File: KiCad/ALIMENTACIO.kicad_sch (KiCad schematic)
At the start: 13 parts, among them J1 Conn_01x02_Pin, U1 LM2596S-5, U2 LM1117DT-3.3

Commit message: Modificacio
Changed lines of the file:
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@@
-	)
-	(junction
-		(at 64.77 99.06)
-		(diameter 0)
-		(color 0 0 0 0)
 	)
 	(junction
@@
 	)
 	(junction
+		(at 60.96 99.06)
+		(diameter 0)
+		(color 0 0 0 0)
+	)
+	(junction
 		(at 176.53 104.14)
+		(diameter 0)
+		(color 0 0 0 0)
+	)
+	(junction
+		(at 60.96 101.6)
 		(diameter 0)
 		(color 0 0 0 0)
@@
 	(wire
 		(pts
-			(xy 57.15 99.06) (xy 64.77 99.06)
+			(xy 57.15 99.06) (xy 60.96 99.06)
 		)
 		(stroke
@@
 	(wire
 		(pts
+			(xy 60.96 101.6) (xy 57.15 101.6)
+		)
+		(stroke
+			(width 0)
+			(type default)
+		)
+	)
+	(wire
+		(pts
 			(xy 245.11 104.14) (xy 259.08 104.14)
 		)
@@
 	(wire
 		(pts
+			(xy 60.96 99.06) (xy 78.74 99.06)
+		)
+		(stroke
+			(width 0)
+			(type default)
+		)
+	)
+	(wire
+		(pts
 			(xy 231.14 111.76) (xy 231.14 119.38)
 		)
@@
 	(wire
 		(pts
+			(xy 64.77 101.6) (xy 60.96 101.6)
+		)
+		(stroke
+			(width 0)
+			(type default)
+		)
+	)
+	(wire
+		(pts
 			(xy 99.06 99.06) (xy 109.22 99.06)
 		)
@@
 		(pts
 			(xy 143.51 99.06) (xy 176.53 99.06)
-		)
-		(stroke
-			(width 0)
-			(type default)
-		)
-	)
-	(wire
-		(pts
-			(xy 64.77 99.06) (xy 78.74 99.06)
 		)
 		(stroke
@@
 	(global_label "GND"
 		(shape input)
-		(at 57.15 101.6 0)
+		(at 64.77 101.6 0)
 		(fields_autoplaced yes)
 		(effects
@@
 		)
 		(property "Intersheetrefs" "${INTERSHEET_REFS}"
-			(at 64.0057 101.6 0)
+			(at 71.6257 101.6 0)
 			(effects
 				(font
@@
 	(symbol
 		(lib_id "power:PWR_FLAG")
-		(at 64.77 99.06 0)
+		(at 60.96 99.06 0)
 		(unit 1)
 		(exclude_from_sim no)
@@
 		(fields_autoplaced yes)
 		(property "Reference" "#FLG01"
-			(at 64.77 97.155 0)
+			(at 60.96 97.155 0)
 			(effects
 				(font
@@
 		)
 		(property "Value" "PWR_FLAG"
-			(at 64.77 93.98 0)
+			(at 60.96 93.98 0)
 			(effects
 				(font
@@
 		)
 		(property "Footprint" ""
-			(at 64.77 99.06 0)
+			(at 60.96 99.06 0)
 			(effects
 				(font
@@
 		)
 		(property "Datasheet" "~"
-			(at 64.77 99.06 0)
+			(at 60.96 99.06 0)
 			(effects
 				(font
@@
 		)
 		(property "Description" "Special symbol for telling ERC where power comes from"
-			(at 64.77 99.06 0)
+			(at 60.96 99.06 0)
 			(effects
 				(font
@@
 					(unit 1)
 				)
+			)
+		)
+	)
+	(symbol
+		(lib_id "power:PWR_FLAG")
+		(at 60.96 101.6 180)
+		(unit 1)
+		(exclude_from_sim no)
+		(in_bom yes)
+		(on_board yes)
+		(dnp no)
+		(fields_autoplaced yes)
+		(property "Reference" "#FLG02"
+			(at 60.96 103.505 0)
+			(effects
+				(font
+					(size 1.27 1.27)
+				)
+				(hide yes)
+			)
+		)
+		(property "Value" "PWR_FLAG"
+			(at 60.96 106.68 0)
+			(effects
+				(font
+					(size 1.27 1.27)
+				)
+			)
+		)
+		(property "Footprint" ""
+			(at 60.96 101.6 0)
+			(effects
+				(font
+					(size 1.27 1.27)
+				)
+				(hide yes)
+			)
+		)
+		(property "Datasheet" "~"
+			(at 60.96 101.6 0)
+			(effects
+				(font
+					(size 1.27 1.27)
+				)
+				(hide yes)
+			)
+		)
+		(property "Description" "Special symbol for telling ERC where power comes from"
+			(at 60.96 101.6 0)
+			(effects
+				(font
+					(size 1.27 1.27)
+				)
+				(hide yes)
+			)
+		)
+		(pin "1"
+		)
+		(instances
+			(project "SEIENTS_EDD"
+				(path "/b6401b4f-5426-49b8-bb2e-8ecdb19989ef/67d546eb-b5d9-4a2c-a3ee-41df96785a31"
+					(reference "#FLG02")
+					(unit 1)
+				)

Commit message: Afegist el MOSFET
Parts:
- renumbered C2 to C1, C5 to C2, C6 to C3, C7 to C4, C3 to C5, C4 to C6, D2 to D1, D1 to D2

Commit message: cambios mejora ERC
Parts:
- renumbered D2 to D1, D1 to D2
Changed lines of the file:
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@@
+	)
+	(junction
+		(at 71.12 99.06)
+		(diameter 0)
+		(color 0 0 0 0)
+	)
+	(junction
+		(at 71.12 95.25)
+		(diameter 0)
+		(color 0 0 0 0)
 	)
 	(junction
@@
 	(wire
 		(pts
-			(xy 57.15 99.06) (xy 78.74 99.06)
+			(xy 57.15 99.06) (xy 71.12 99.06)
 		)
 		(stroke
@@
 	(wire
 		(pts
+			(xy 71.12 99.06) (xy 78.74 99.06)
+		)
+		(stroke
+			(width 0)
+			(type default)
+		)
+	)
+	(wire
+		(pts
+			(xy 71.12 95.25) (xy 71.12 99.06)
+		)
+		(stroke
+			(width 0)
+			(type default)
+		)
+	)
+	(wire
+		(pts
 			(xy 109.22 104.14) (xy 118.11 104.14)
 		)
@@
 	(wire
 		(pts
+			(xy 71.12 93.98) (xy 71.12 95.25)
+		)
+		(stroke
+			(width 0)
+			(type default)
+		)
+	)
+	(wire
+		(pts
 			(xy 245.11 104.14) (xy 245.11 107.95)
 		)
@@
 	)
 	(global_label "+5V"
-		(shape input)
+		(shape bidirectional)
 		(at 176.53 99.06 90)
 		(fields_autoplaced yes)
@@
 		)
 		(property "Intersheetrefs" "${INTERSHEET_REFS}"
-			(at 176.53 92.2043 90)
+			(at 176.53 91.093 90)
 			(effects
 				(font
@@
 	(global_label "VBAT"
 		(shape input)
-		(at 71.12 99.06 90)
+		(at 71.12 93.98 90)
 		(fields_autoplaced yes)
 		(effects
@@
 		)
 		(property "Intersheetrefs" "${INTERSHEET_REFS}"
-			(at 71.12 91.66 90)
+			(at 71.12 86.58 90)
 			(effects
 				(font
@@
 	)
 	(global_label "+3.3V"
-		(shape input)
+		(shape output)
 		(at 259.08 104.14 0)
 		(fields_autoplaced yes)
@@
 			(project "SEIENTS_EDD"
 				(path "/b6401b4f-5426-49b8-bb2e-8ecdb19989ef/67d546eb-b5d9-4a2c-a3ee-41df96785a31"
-					(reference "C5")
+					(reference "C2")
 					(unit 1)
 				)
@@
 			(project ""
 				(path "/b6401b4f-5426-49b8-bb2e-8ecdb19989ef/67d546eb-b5d9-4a2c-a3ee-41df96785a31"
-					(reference "C3")
+					(reference "C5")
 					(unit 1)
 				)
@@
 		(dnp no)
 		(fields_autoplaced yes)
-		(property "Reference" "D2"
+		(property "Reference" "D1"
 			(at 95.25 92.71 0)
 			(effects
@@
 		(dnp no)
 		(fields_autoplaced yes)
-		(property "Reference" "#PWR05"
+		(property "Reference" "#PWR06"
 			(at 176.53 125.73 0)
 			(effects
@@
 				)
 			)
+			(project "SEIENTS_EDD"
+				(path "/b6401b4f-5426-49b8-bb2e-8ecdb19989ef/67d546eb-b5d9-4a2c-a3ee-41df96785a31"
+					(reference "#PWR06")
+					(unit 1)
+				)
+			)
 		)
 	)
@@
 		(dnp no)
 		(fields_autoplaced yes)
-		(property "Reference" "D1"
+		(property "Reference" "D2"
 			(at 147.32 115.8876 90)
 			(effects
@@
 		(dnp no)
 		(fields_autoplaced yes)
-		(property "Reference" "#PWR02"
+		(property "Reference" "#PWR03"
 			(at 109.22 125.73 0)
 			(effects
@@
 				)
 			)
+			(project "SEIENTS_EDD"
+				(path "/b6401b4f-5426-49b8-bb2e-8ecdb19989ef/67d546eb-b5d9-4a2c-a3ee-41df96785a31"
+					(reference "#PWR03")
+					(unit 1)
+				)
+			)
+		)
+	)
+	(symbol
+		(lib_id "power:PWR_FLAG")
+		(at 71.12 95.25 90)
+		(unit 1)
+		(exclude_from_sim no)
+		(in_bom yes)
+		(on_board yes)
+		(dnp no)
+		(fields_autoplaced yes)
+		(property "Reference" "#FLG02"
+			(at 69.215 95.25 0)
+			(effects
+				(font
+					(size 1.27 1.27)
+				)
+				(hide yes)
+			)
+		)
+		(property "Value" "PWR_FLAG"
+			(at 67.31 95.2499 90)
+			(effects
+				(font
+					(size 1.27 1.27)
+				)
+				(justify left)
+			)
+		)
+		(property "Footprint" ""
+			(at 71.12 95.25 0)
+			(effects
+				(font
+					(size 1.27 1.27)
+				)
+				(hide yes)
+			)
+		)
+		(property "Datasheet" "~"
+			(at 71.12 95.25 0)
+			(effects
+				(font
+					(size 1.27 1.27)
+				)
+				(hide yes)
+			)
+		)
+		(property "Description" "Special symbol for telling ERC where power comes from"
+			(at 71.12 95.25 0)
+			(effects
+				(font
+					(size 1.27 1.27)
+				)
+				(hide yes)
+			)
+		)
+		(pin "1"
+		)
+		(instances
+			(project "ALIMENTACIO"
+				(path "/45cfcaa5-e694-40cb-923c-70f0cad76365"
+					(reference "#FLG02")
+					(unit 1)
+				)
+			)
+			(project "SEIENTS_EDD"
+				(path "/b6401b4f-5426-49b8-bb2e-8ecdb19989ef/67d546eb-b5d9-4a2c-a3ee-41df96785a31"
+					(reference "#FLG02")
+					(unit 1)
+				)
+			)
 		)
 	)
@@
 		(dnp no)
 		(fields_autoplaced yes)
-		(property "Reference" "#FLG03"
+		(property "Reference" "#FLG04"
 			(at 223.52 102.235 0)
 			(effects
@@
 			(project "SEIENTS_EDD"
 				(path "/b6401b4f-5426-49b8-bb2e-8ecdb19989ef/67d546eb-b5d9-4a2c-a3ee-41df96785a31"
-					(reference "#FLG0101")
+					(reference "#FLG04")
 					(unit 1)
 				)
@@
 		(dnp no)
 		(fields_autoplaced yes)
-		(property "Reference" "#PWR08"
+		(property "Reference" "#PWR09"
 			(at 245.11 125.73 0)
 			(effects
@@
 				)
 			)
+			(project "SEIENTS_EDD"
+				(path "/b6401b4f-5426-49b8-bb2e-8ecdb19989ef/67d546eb-b5d9-4a2c-a3ee-41df96785a31"
+					(reference "#PWR09")
+					(unit 1)
+				)
+			)
 		)
 	)
@@
 		(dnp no)
 		(fields_autoplaced yes)
-		(property "Reference" "#PWR07"
+		(property "Reference" "#PWR08"
 			(at 231.14 125.73 0)
 			(effects
@@
 				)
 			)
+			(project "SEIENTS_EDD"
+				(path "/b6401b4f-5426-49b8-bb2e-8ecdb19989ef/67d546eb-b5d9-4a2c-a3ee-41df96785a31"
+					(reference "#PWR08")
+					(unit 1)
+				)
+			)
 		)
 	)
@@
 		(dnp no)
 		(fields_autoplaced yes)
-		(property "Reference" "#PWR03"
+		(property "Reference" "#PWR04"
 			(at 130.81 125.73 0)
 			(effects
@@
 				)
 			)
+			(project "SEIENTS_EDD"
+				(path "/b6401b4f-5426-49b8-bb2e-8ecdb19989ef/67d546eb-b5d9-4a2c-a3ee-41df96785a31"
+					(reference "#PWR04")
+					(unit 1)
+				)
+			)
 		)
 	)
@@
 			(project "SEIENTS_EDD"
 				(path "/b6401b4f-5426-49b8-bb2e-8ecdb19989ef/67d546eb-b5d9-4a2c-a3ee-41df96785a31"
-					(reference "C4")
+					(reference "C6")
 					(unit 1)
 				)
@@
 			(project "SEIENTS_EDD"
 				(path "/b6401b4f-5426-49b8-bb2e-8ecdb19989ef/67d546eb-b5d9-4a2c-a3ee-41df96785a31"
-					(reference "C2")
+					(reference "C1")
 					(unit 1)
 				)
@@
 				)
 			)
+			(project "SEIENTS_EDD"
+				(path "/b6401b4f-5426-49b8-bb2e-8ecdb19989ef/67d546eb-b5d9-4a2c-a3ee-41df96785a31"
+					(reference "#PWR01")
+					(unit 1)
+				)
+			)
 		)
 	)
@@
 			(project "SEIENTS_EDD"
 				(path "/b6401b4f-5426-49b8-bb2e-8ecdb19989ef/67d546eb-b5d9-4a2c-a3ee-41df96785a31"
-					(reference "C7")
+					(reference "C4")
 					(unit 1)
 				)
@@
 		(dnp no)
 		(fields_autoplaced yes)
-		(property "Reference" "#PWR06"
+		(property "Reference" "#PWR07"
 			(at 215.9 125.73 0)
 			(effects
@@
 				)
 			)
+			(project "SEIENTS_EDD"
+				(path "/b6401b4f-5426-49b8-bb2e-8ecdb19989ef/67d546eb-b5d9-4a2c-a3ee-41df96785a31"
+					(reference "#PWR07")
+					(unit 1)
+				)
+			)
 		)
 	)
@@
 		(dnp no)
 		(fields_autoplaced yes)
-		(property "Reference" "#PWR04"
+		(property "Reference" "#PWR05"
 			(at 149.86 133.35 0)
 			(effects
@@
 				)
 			)
+			(project "SEIENTS_EDD"
+				(path "/b6401b4f-5426-49b8-bb2e-8ecdb19989ef/67d546eb-b5d9-4a2c-a3ee-41df96785a31"
+					(reference "#PWR05")
+					(unit 1)
+				)
+			)
 		)
 	)
@@
 		(dnp no)
 		(fields_autoplaced yes)
-		(property "Reference" "#FLG0102"
+		(property "Reference" "#FLG01"
 			(at 60.96 103.505 0)
 			(effects
@@
 			(project "SEIENTS_EDD"
 				(path "/b6401b4f-5426-49b8-bb2e-8ecdb19989ef/67d546eb-b5d9-4a2c-a3ee-41df96785a31"
-					(reference "#FLG02")
+					(reference "#FLG01")
 					(unit 1)
 				)
@@
 		(dnp no)
 		(fields_autoplaced yes)
-		(property "Reference" "#FLG01"
+		(property "Reference" "#FLG03"
 			(at 118.11 97.155 0)
 			(effects
@@
 			(project "SEIENTS_EDD"
 				(path "/b6401b4f-5426-49b8-bb2e-8ecdb19989ef/67d546eb-b5d9-4a2c-a3ee-41df96785a31"
-					(reference "#FLG0102")
+					(reference "#FLG03")
 					(unit 1)
 				)
@@
 		(dnp no)
 		(fields_autoplaced yes)
-		(property "Reference" "#PWR09"
+		(property "Reference" "#PWR02"
 			(at 109.22 62.23 0)
 			(effects
@@
 				)
 			)
+			(project "SEIENTS_EDD"
+				(path "/b6401b4f-5426-49b8-bb2e-8ecdb19989ef/67d546eb-b5d9-4a2c-a3ee-41df96785a31"
+					(reference "#PWR02")
+					(unit 1)
+				)
+			)
 		)
 	)
@@
 			(project "SEIENTS_EDD"
 				(path "/b6401b4f-5426-49b8-bb2e-8ecdb19989ef/67d546eb-b5d9-4a2c-a3ee-41df96785a31"
-					(reference "C6")
-					(unit 1)
-				)
+					(reference "C3")
+					(unit 1)
+				)

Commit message: Començat el LAYOUT
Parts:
- D1: footprint (none) -> Diode_SMD:D_SMA
- F1: footprint (none) -> Fuse:Fuseholder_Cylinder-5x20mm_Schurter_0031_8201_Horizontal_Open
- L1: footprint (none) -> Inductor_THT:L_Radial_D10.0mm_P5.00mm_Fastron_07M
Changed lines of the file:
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@@
 			)
 		)
-		(property "Footprint" ""
+		(property "Footprint" "Diode_SMD:D_SMA"
 			(at 95.25 99.06 0)
 			(effects
@@
 			)
 		)
-		(property "Footprint" ""
+		(property "Footprint" "Fuse:Fuseholder_Cylinder-5x20mm_Schurter_0031_8201_Horizontal_Open"
 			(at 82.55 100.838 90)
 			(effects
@@
 			)
 		)
-		(property "Footprint" ""
+		(property "Footprint" "Inductor_THT:L_Radial_D10.0mm_P5.00mm_Fastron_07M"
 			(at 165.1 104.14 0)
 			(effects

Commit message: footprints asignados
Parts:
- C1, C2, C3, C4, C5, C6: footprint (none) -> Capacitor_SMD:C_0805_2012Metric
- J1: footprint (none) -> Connector_PinHeader_2.54mm:PinHeader_1x02_P2.54mm_Vertical
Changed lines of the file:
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@@
 			)
 		)
-		(property "Footprint" ""
+		(property "Footprint" "Capacitor_SMD:C_0805_2012Metric"
 			(at 110.1852 86.36 0)
 			(effects
@@
 			)
 		)
-		(property "Footprint" ""
+		(property "Footprint" "Capacitor_SMD:C_0805_2012Metric"
 			(at 216.8652 115.57 0)
 			(effects
@@
 			)
 		)
-		(property "Footprint" ""
+		(property "Footprint" "Connector_PinHeader_2.54mm:PinHeader_1x02_P2.54mm_Vertical"
 			(at 52.07 99.06 0)
 			(effects
@@
 			)
 		)
-		(property "Footprint" ""
+		(property "Footprint" "Capacitor_SMD:C_0805_2012Metric"
 			(at 246.0752 115.57 0)
 			(effects
@@
 			)
 		)
-		(property "Footprint" ""
+		(property "Footprint" "Capacitor_SMD:C_0805_2012Metric"
 			(at 101.2952 86.36 0)
 			(effects
@@
 			)
 		)
-		(property "Footprint" ""
+		(property "Footprint" "Capacitor_SMD:C_0805_2012Metric"
 			(at 190.1952 115.57 0)
 			(effects
@@
 			)
 		)
-		(property "Footprint" ""
+		(property "Footprint" "Capacitor_SMD:C_0805_2012Metric"
 			(at 177.4952 115.57 0)
 			(effects

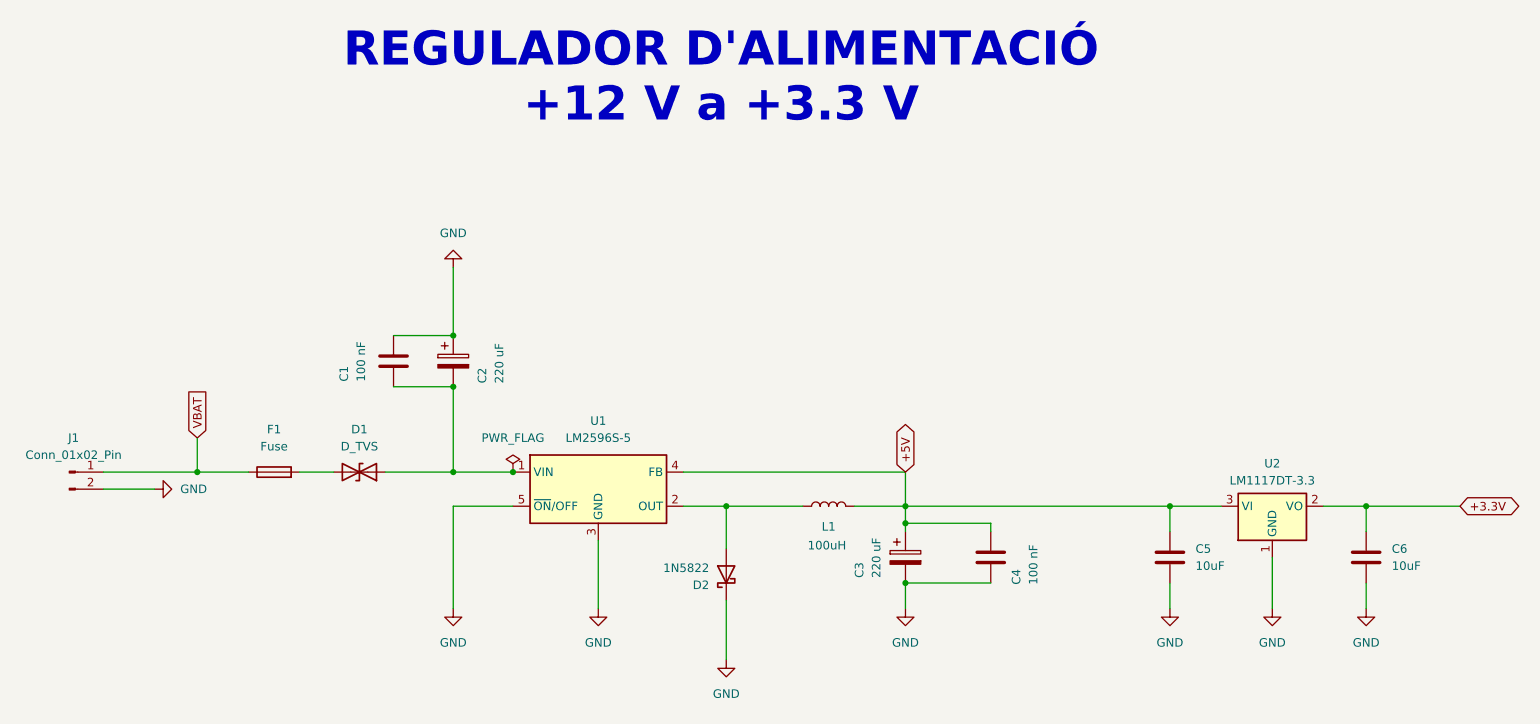
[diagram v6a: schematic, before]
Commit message: Testpoint añadidos
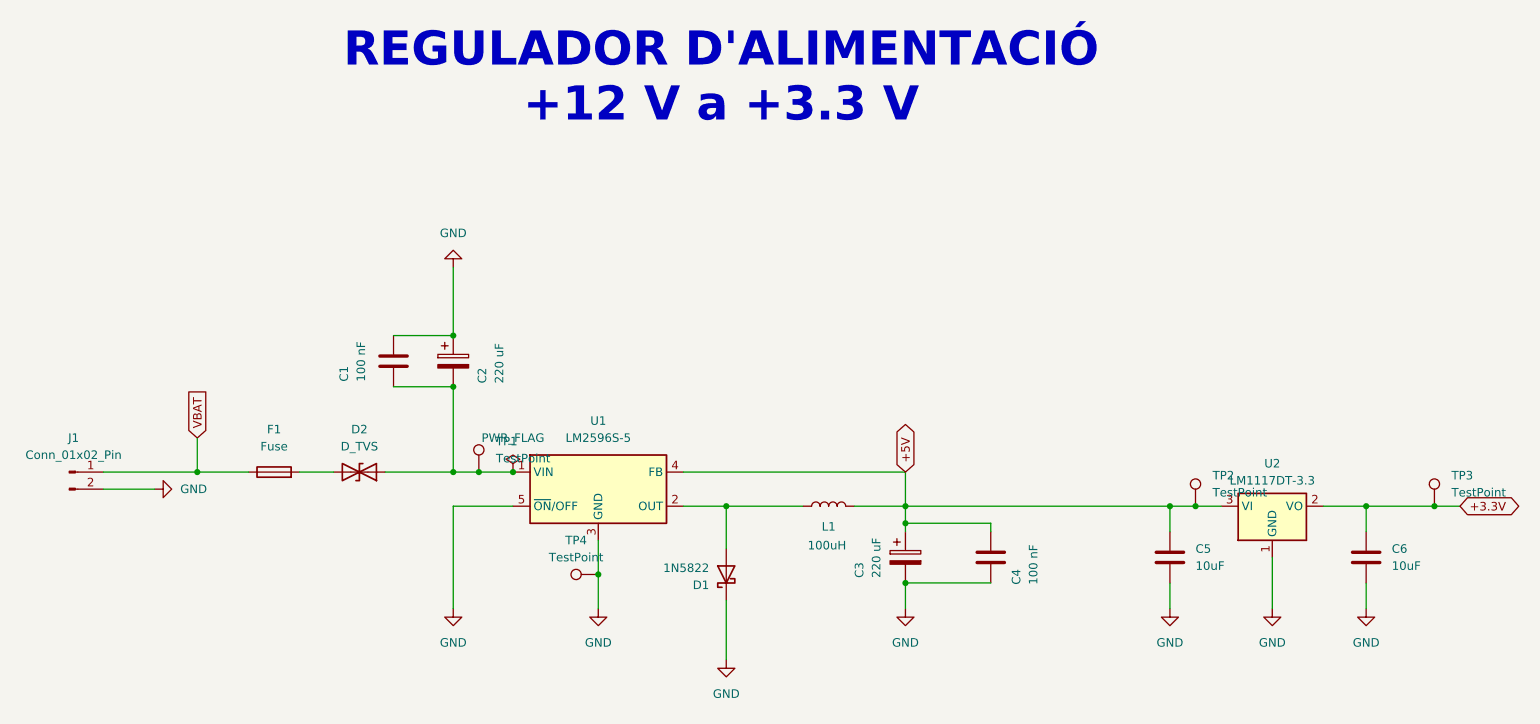
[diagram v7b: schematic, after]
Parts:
- added TP1, TP2, TP3, TP4: TestPoint, symbol Connector:TestPoint
- renumbered D2 to D1, D1 to D2
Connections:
- net +3.3V: now also TP3.1
- net +5V: now also TP2.1
- net GND: now also TP4.1
- net at C1.2, C2.2, D2.1 (A1)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: now also TP1.1

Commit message: Modificat ETIQUETES MICROCONTROLADOR
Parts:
- renumbered D2 to D1, D1 to D2
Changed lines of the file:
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@@
 		(dnp no)
 		(fields_autoplaced yes)
-		(property "Reference" "TP4"
+		(property "Reference" "TP?"
 			(at 127.508 109.22 90)
 			(effects
@@
 				)
 			)
+			(project "SEIENTS_EDD"
+				(path "/b6401b4f-5426-49b8-bb2e-8ecdb19989ef/67d546eb-b5d9-4a2c-a3ee-41df96785a31"
+					(reference "TP?")
+					(unit 1)
+				)
+			)
 		)
 	)
@@
 		(dnp no)
 		(fields_autoplaced yes)
-		(property "Reference" "D2"
+		(property "Reference" "D1"
 			(at 95.25 92.71 0)
 			(effects
@@
 		(dnp no)
 		(fields_autoplaced yes)
-		(property "Reference" "TP3"
+		(property "Reference" "TP?"
 			(at 257.81 99.5679 0)
 			(effects
@@
 				)
 			)
+			(project "SEIENTS_EDD"
+				(path "/b6401b4f-5426-49b8-bb2e-8ecdb19989ef/67d546eb-b5d9-4a2c-a3ee-41df96785a31"
+					(reference "TP?")
+					(unit 1)
+				)
+			)
 		)
 	)
@@
 		(dnp no)
 		(fields_autoplaced yes)
-		(property "Reference" "#PWR05"
+		(property "Reference" "#PWR06"
 			(at 176.53 125.73 0)
 			(effects
@@
 		(dnp no)
 		(fields_autoplaced yes)
-		(property "Reference" "D1"
+		(property "Reference" "D2"
 			(at 147.32 115.8876 90)
 			(effects
@@
 		(dnp no)
 		(fields_autoplaced yes)
-		(property "Reference" "#PWR02"
+		(property "Reference" "#PWR03"
 			(at 109.22 125.73 0)
 			(effects
@@
 		(dnp no)
 		(fields_autoplaced yes)
-		(property "Reference" "TP1"
+		(property "Reference" "TP?"
 			(at 115.57 94.4879 0)
 			(effects
@@
 				)
 			)
+			(project "SEIENTS_EDD"
+				(path "/b6401b4f-5426-49b8-bb2e-8ecdb19989ef/67d546eb-b5d9-4a2c-a3ee-41df96785a31"
+					(reference "TP?")
+					(unit 1)
+				)
+			)
 		)
 	)
@@
 		(dnp no)
 		(fields_autoplaced yes)
-		(property "Reference" "#PWR08"
+		(property "Reference" "#PWR09"
 			(at 245.11 125.73 0)
 			(effects
@@
 		(dnp no)
 		(fields_autoplaced yes)
-		(property "Reference" "#PWR07"
+		(property "Reference" "#PWR08"
 			(at 231.14 125.73 0)
 			(effects
@@
 		(dnp no)
 		(fields_autoplaced yes)
-		(property "Reference" "#PWR03"
+		(property "Reference" "#PWR04"
 			(at 130.81 125.73 0)
 			(effects
@@
 		(dnp no)
 		(fields_autoplaced yes)
-		(property "Reference" "TP2"
+		(property "Reference" "TP?"
 			(at 222.25 99.5679 0)
 			(effects
@@
 				)
 			)
+			(project "SEIENTS_EDD"
+				(path "/b6401b4f-5426-49b8-bb2e-8ecdb19989ef/67d546eb-b5d9-4a2c-a3ee-41df96785a31"
+					(reference "TP?")
+					(unit 1)
+				)
+			)
 		)
 	)
@@
 		(dnp no)
 		(fields_autoplaced yes)
-		(property "Reference" "#PWR06"
+		(property "Reference" "#PWR07"
 			(at 215.9 125.73 0)
 			(effects
@@
 		(dnp no)
 		(fields_autoplaced yes)
-		(property "Reference" "#PWR04"
+		(property "Reference" "#PWR05"
 			(at 149.86 133.35 0)
 			(effects
@@
 		(dnp no)
 		(fields_autoplaced yes)
-		(property "Reference" "#FLG01"
+		(property "Reference" "#FLG03"
 			(at 118.11 97.155 0)
 			(effects
@@
 		(dnp no)
 		(fields_autoplaced yes)
-		(property "Reference" "#PWR09"
+		(property "Reference" "#PWR02"
 			(at 109.22 62.23 0)
 			(effects
